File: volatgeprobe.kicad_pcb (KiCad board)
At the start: 2 copper layers, 106.9 x 49.2 mm, 52 parts, among them IC1 AMC1301SDWV, J1 Conn_01x01_Male, J2 Conn_01x01_Male, J3 Conn_01x02_Male, J4 Conn_Coaxial, SW1 SW_SPST, U1 AZ1117IH-3.3TRG1, U2 5-15v, U4 LF353M, U5 LF353M

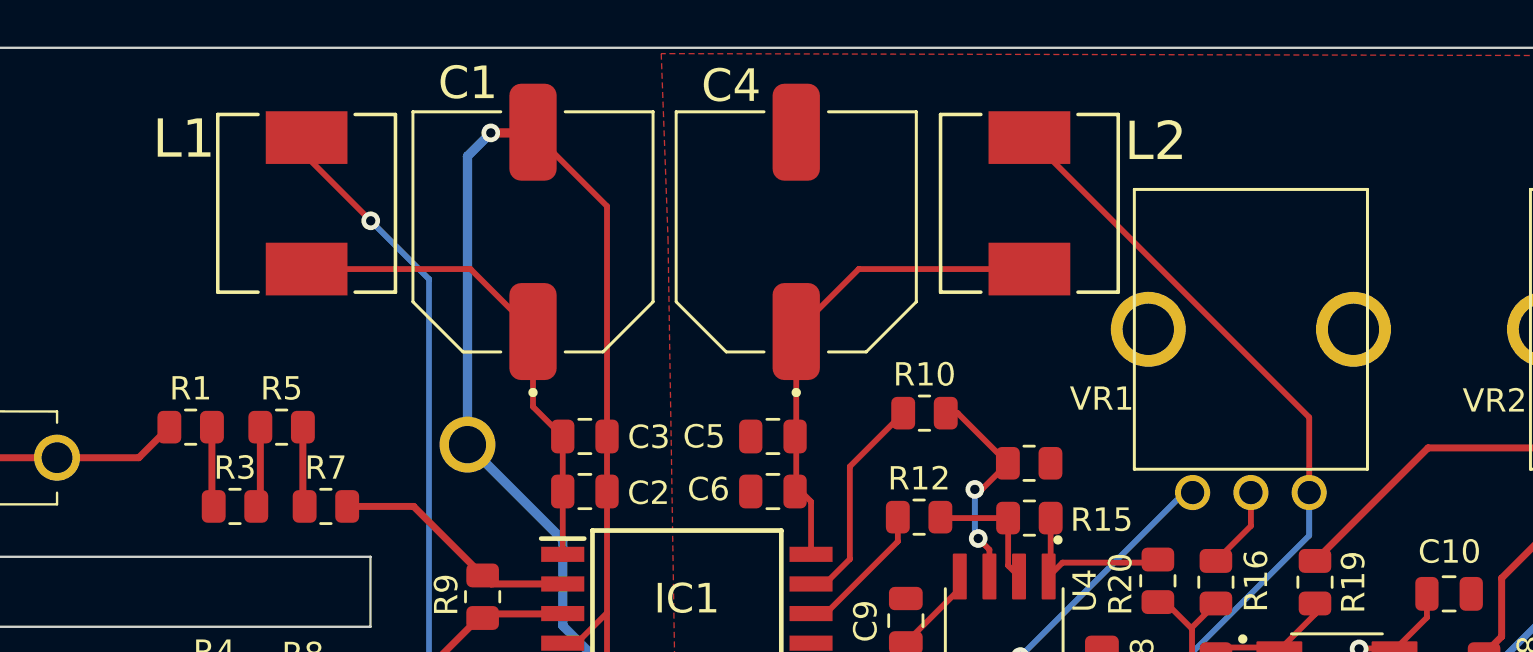
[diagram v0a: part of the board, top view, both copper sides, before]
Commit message: inductors foot print changed
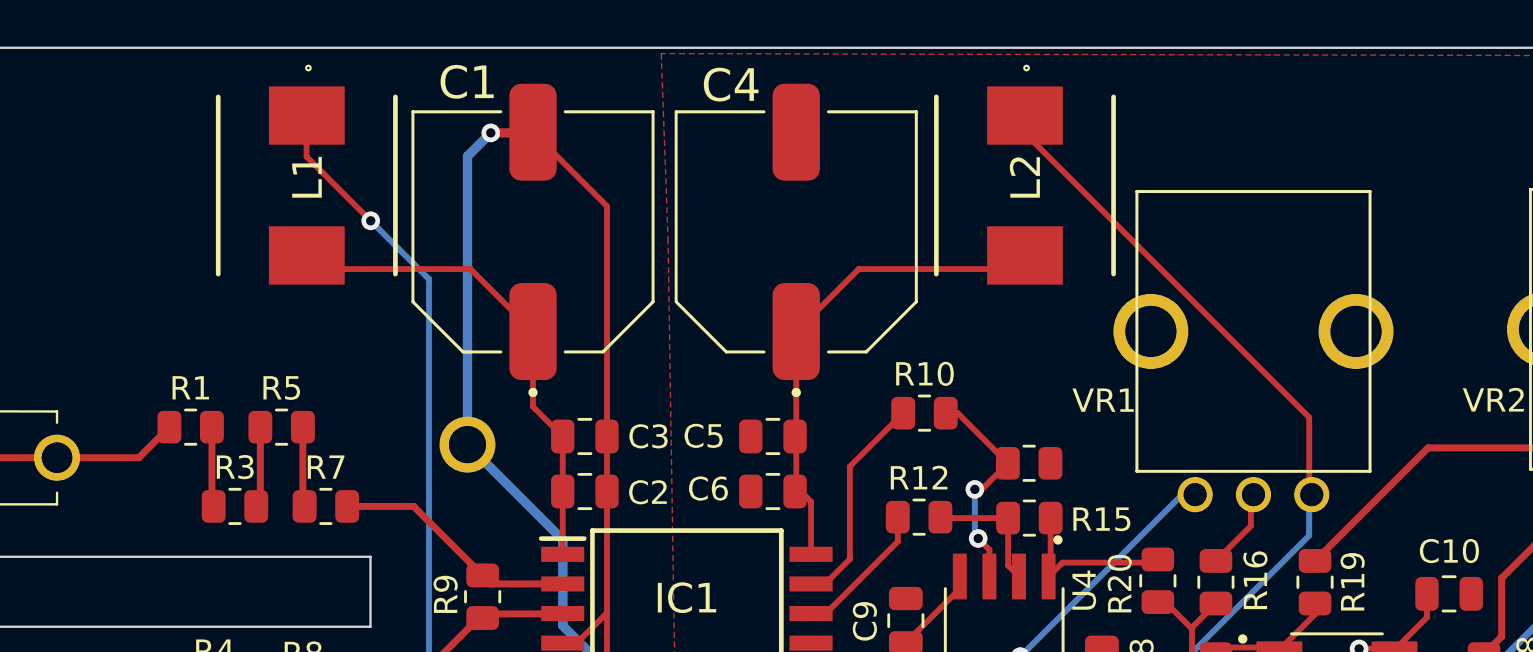
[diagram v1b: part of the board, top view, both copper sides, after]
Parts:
- L1, L2: footprint inductor:INDM7676X435N -> inductor:DR74
- moved L2 0.79 mm to (150.8, 85.8)
- moved L1 0.76 mm to (120.0, 85.8)
- moved VR1 0.14 mm to (160.6, 99.1)
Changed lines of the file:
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@@
   )
   (footprint "trim:PTV09" (layer "F.Cu")
-    (at 160.51625 99.01475)
+    (at 160.62625 99.10475)
     (property "PARTNO" "PTV09A-4225F-B104-ND")
     (property "Sheetfile" "volatgeprobe.kicad_sch")
@@
     )
   )
-  (footprint "inductor:INDM7676X435N" (layer "F.Cu")
-    (at 120.01625 86.61 -90)
+  (footprint "inductor:DR74" (layer "F.Cu")
+    (at 120.02625 85.846 -90)
+    (descr "DR74")
+    (tags "Inductor")
     (property "Sheetfile" "volatgeprobe.kicad_sch")
     (property "Sheetname" "")
@@
     (property "ki_keywords" "simulation")
     (attr smd)
-    (fp_text reference "L1" (at -2.76 5.26 -180) (layer "F.SilkS")
-        (effects (font (size 1.643331 1.643331) (thickness 0.15)))
-    )
-    (fp_text value "1mH" (at 8.12842 5.60583 90) (layer "F.Fab")
-        (effects (font (size 1.645228 1.645228) (thickness 0.15)))
-    )
-    (fp_line (start -3.81 -3.81) (end -3.81 -2.0828)
-      (stroke (width 0.1524) (type solid)) (layer "F.SilkS"))
-    (fp_line (start -3.81 2.0828) (end -3.81 3.81)
-      (stroke (width 0.1524) (type solid)) (layer "F.SilkS"))
-    (fp_line (start -3.81 3.81) (end 3.81 3.81)
-      (stroke (width 0.1524) (type solid)) (layer "F.SilkS"))
-    (fp_line (start 3.81 -3.81) (end -3.81 -3.81)
-      (stroke (width 0.1524) (type solid)) (layer "F.SilkS"))
-    (fp_line (start 3.81 -2.0828) (end 3.81 -3.81)
-      (stroke (width 0.1524) (type solid)) (layer "F.SilkS"))
-    (fp_line (start 3.81 3.81) (end 3.81 2.0828)
-      (stroke (width 0.1524) (type solid)) (layer "F.SilkS"))
-    (fp_line (start -3.81 -3.81) (end -3.81 3.81)
-      (stroke (width 0.1524) (type solid)) (layer "F.Fab"))
-    (fp_line (start -3.81 -1.905) (end -1.905 -3.81)
-      (stroke (width 0.1524) (type solid)) (layer "F.Fab"))
-    (fp_line (start -3.81 1.905) (end -1.905 3.81)
-      (stroke (width 0.1524) (type solid)) (layer "F.Fab"))
-    (fp_line (start -3.81 3.81) (end 3.81 3.81)
-      (stroke (width 0.1524) (type solid)) (layer "F.Fab"))
-    (fp_line (start 3.81 -3.81) (end -3.81 -3.81)
-      (stroke (width 0.1524) (type solid)) (layer "F.Fab"))
-    (fp_line (start 3.81 3.81) (end 3.81 -3.81)
-      (stroke (width 0.1524) (type solid)) (layer "F.Fab"))
-    (pad "1" smd rect (at -2.8194 0) (size 3.5052 2.2606) (layers "F.Cu" "F.Paste" "F.Mask")
+    (fp_text reference "L1" (at -0.347 -0.054 -90) (layer "F.SilkS")
+        (effects (font (size 1.27 1.27) (thickness 0.254)))
+    )
+    (fp_text value "1mH" (at -0.347 -0.054 -90) (layer "F.SilkS") hide
+        (effects (font (size 1.27 1.27) (thickness 0.254)))
+    )
+    (fp_text user "${REFERENCE}" (at -0.347 -0.054 -90) (layer "F.Fab")
+        (effects (font (size 1.27 1.27) (thickness 0.254)))
+    )
+    (fp_line (start -3.8 -3.8) (end 3.8 -3.8)
+      (stroke (width 0.2) (type solid)) (layer "F.SilkS"))
+    (fp_line (start 3.8 3.8) (end -3.8 3.8)
+      (stroke (width 0.2) (type solid)) (layer "F.SilkS"))
+    (fp_circle (center -5.038 -0.068) (end -5.038 -0.024)
+      (stroke (width 0.2) (type solid)) (fill none) (layer "F.SilkS"))
+    (fp_line (start -3.8 -3.8) (end 3.8 -3.8)
+      (stroke (width 0.2) (type solid)) (layer "F.Fab"))
+    (fp_line (start -3.8 3.8) (end -3.8 -3.8)
+      (stroke (width 0.2) (type solid)) (layer "F.Fab"))
+    (fp_line (start 3.8 -3.8) (end 3.8 3.8)
+      (stroke (width 0.2) (type solid)) (layer "F.Fab"))
+    (fp_line (start 3.8 3.8) (end -3.8 3.8)
+      (stroke (width 0.2) (type solid)) (layer "F.Fab"))
+    (pad "1" smd rect (at -3 0 270) (size 2.5 3.25) (layers "F.Cu" "F.Paste" "F.Mask")
       (net 7 "+5V_re") (pinfunction "1") (pintype "input"))
-    (pad "2" smd rect (at 2.8194 0) (size 3.5052 2.2606) (layers "F.Cu" "F.Paste" "F.Mask")
+    (pad "2" smd rect (at 3 0 270) (size 2.5 3.25) (layers "F.Cu" "F.Paste" "F.Mask")
       (net 1 "+5V") (pinfunction "2") (pintype "input"))
   )
@@
     )
   )
-  (footprint "inductor:INDM7676X435N" (layer "F.Cu")
-    (at 151.01625 86.61 -90)
+  (footprint "inductor:DR74" (layer "F.Cu")
+    (at 150.82625 85.846 -90)
+    (descr "DR74")
+    (tags "Inductor")
     (property "Sheetfile" "volatgeprobe.kicad_sch")
     (property "Sheetname" "")
@@
     (property "ki_keywords" "simulation")
     (attr smd)
-    (fp_text reference "L2" (at -2.66 -5.42 -180) (layer "F.SilkS")
-        (effects (font (size 1.643331 1.643331) (thickness 0.15)))
-    )
-    (fp_text value "1mH" (at 8.12842 5.60583 -270) (layer "F.Fab")
-        (effects (font (size 1.645228 1.645228) (thickness 0.15)))
-    )
-    (fp_line (start -3.81 -3.81) (end -3.81 -2.0828)
-      (stroke (width 0.1524) (type solid)) (layer "F.SilkS"))
-    (fp_line (start -3.81 2.0828) (end -3.81 3.81)
-      (stroke (width 0.1524) (type solid)) (layer "F.SilkS"))
-    (fp_line (start -3.81 3.81) (end 3.81 3.81)
-      (stroke (width 0.1524) (type solid)) (layer "F.SilkS"))
-    (fp_line (start 3.81 -3.81) (end -3.81 -3.81)
-      (stroke (width 0.1524) (type solid)) (layer "F.SilkS"))
-    (fp_line (start 3.81 -2.0828) (end 3.81 -3.81)
-      (stroke (width 0.1524) (type solid)) (layer "F.SilkS"))
-    (fp_line (start 3.81 3.81) (end 3.81 2.0828)
-      (stroke (width 0.1524) (type solid)) (layer "F.SilkS"))
-    (fp_line (start -3.81 -3.81) (end -3.81 3.81)
-      (stroke (width 0.1524) (type solid)) (layer "F.Fab"))
-    (fp_line (start -3.81 -1.905) (end -1.905 -3.81)
-      (stroke (width 0.1524) (type solid)) (layer "F.Fab"))
-    (fp_line (start -3.81 1.905) (end -1.905 3.81)
-      (stroke (width 0.1524) (type solid)) (layer "F.Fab"))
-    (fp_line (start -3.81 3.81) (end 3.81 3.81)
-      (stroke (width 0.1524) (type solid)) (layer "F.Fab"))
-    (fp_line (start 3.81 -3.81) (end -3.81 -3.81)
-      (stroke (width 0.1524) (type solid)) (layer "F.Fab"))
-    (fp_line (start 3.81 3.81) (end 3.81 -3.81)
-      (stroke (width 0.1524) (type solid)) (layer "F.Fab"))
-    (pad "1" smd rect (at -2.8194 0) (size 3.5052 2.2606) (layers "F.Cu" "F.Paste" "F.Mask")
+    (fp_text reference "L2" (at -0.347 -0.054 -90) (layer "F.SilkS")
+        (effects (font (size 1.27 1.27) (thickness 0.254)))
+    )
+    (fp_text value "1mH" (at -0.347 -0.054 -90) (layer "F.SilkS") hide
+        (effects (font (size 1.27 1.27) (thickness 0.254)))
+    )
+    (fp_text user "${REFERENCE}" (at -0.347 -0.054 -90) (layer "F.Fab")
+        (effects (font (size 1.27 1.27) (thickness 0.254)))
+    )
+    (fp_line (start -3.8 -3.8) (end 3.8 -3.8)
+      (stroke (width 0.2) (type solid)) (layer "F.SilkS"))
+    (fp_line (start 3.8 3.8) (end -3.8 3.8)
+      (stroke (width 0.2) (type solid)) (layer "F.SilkS"))
+    (fp_circle (center -5.038 -0.068) (end -5.038 -0.024)
+      (stroke (width 0.2) (type solid)) (fill none) (layer "F.SilkS"))
+    (fp_line (start -3.8 -3.8) (end 3.8 -3.8)
+      (stroke (width 0.2) (type solid)) (layer "F.Fab"))
+    (fp_line (start -3.8 3.8) (end -3.8 -3.8)
+      (stroke (width 0.2) (type solid)) (layer "F.Fab"))
+    (fp_line (start 3.8 -3.8) (end 3.8 3.8)
+      (stroke (width 0.2) (type solid)) (layer "F.Fab"))
+    (fp_line (start 3.8 3.8) (end -3.8 3.8)
+      (stroke (width 0.2) (type solid)) (layer "F.Fab"))
+    (pad "1" smd rect (at -3 0 270) (size 2.5 3.25) (layers "F.Cu" "F.Paste" "F.Mask")
       (net 8 "+5V_le") (pinfunction "1") (pintype "input"))
-    (pad "2" smd rect (at 2.8194 0) (size 3.5052 2.2606) (layers "F.Cu" "F.Paste" "F.Mask")
+    (pad "2" smd rect (at 3 0 270) (size 2.5 3.25) (layers "F.Cu" "F.Paste" "F.Mask")
       (net 3 "+5V-a") (pinfunction "2") (pintype "input"))
   )
